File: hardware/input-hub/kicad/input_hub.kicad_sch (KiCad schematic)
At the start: 29 parts, among them J1 ACJMIH, J12 PJ-307, J13 PJ-307, J2 ACJMIH, J5 54602-908LF, J6 BM04B-SRSS-TB_LF__SN_, J7 Conn_01x04, J8 Conn_01x02, J9 XIAO_BAT_SOLDER_ACCESS, P1 B2B-PH-SM4-TB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

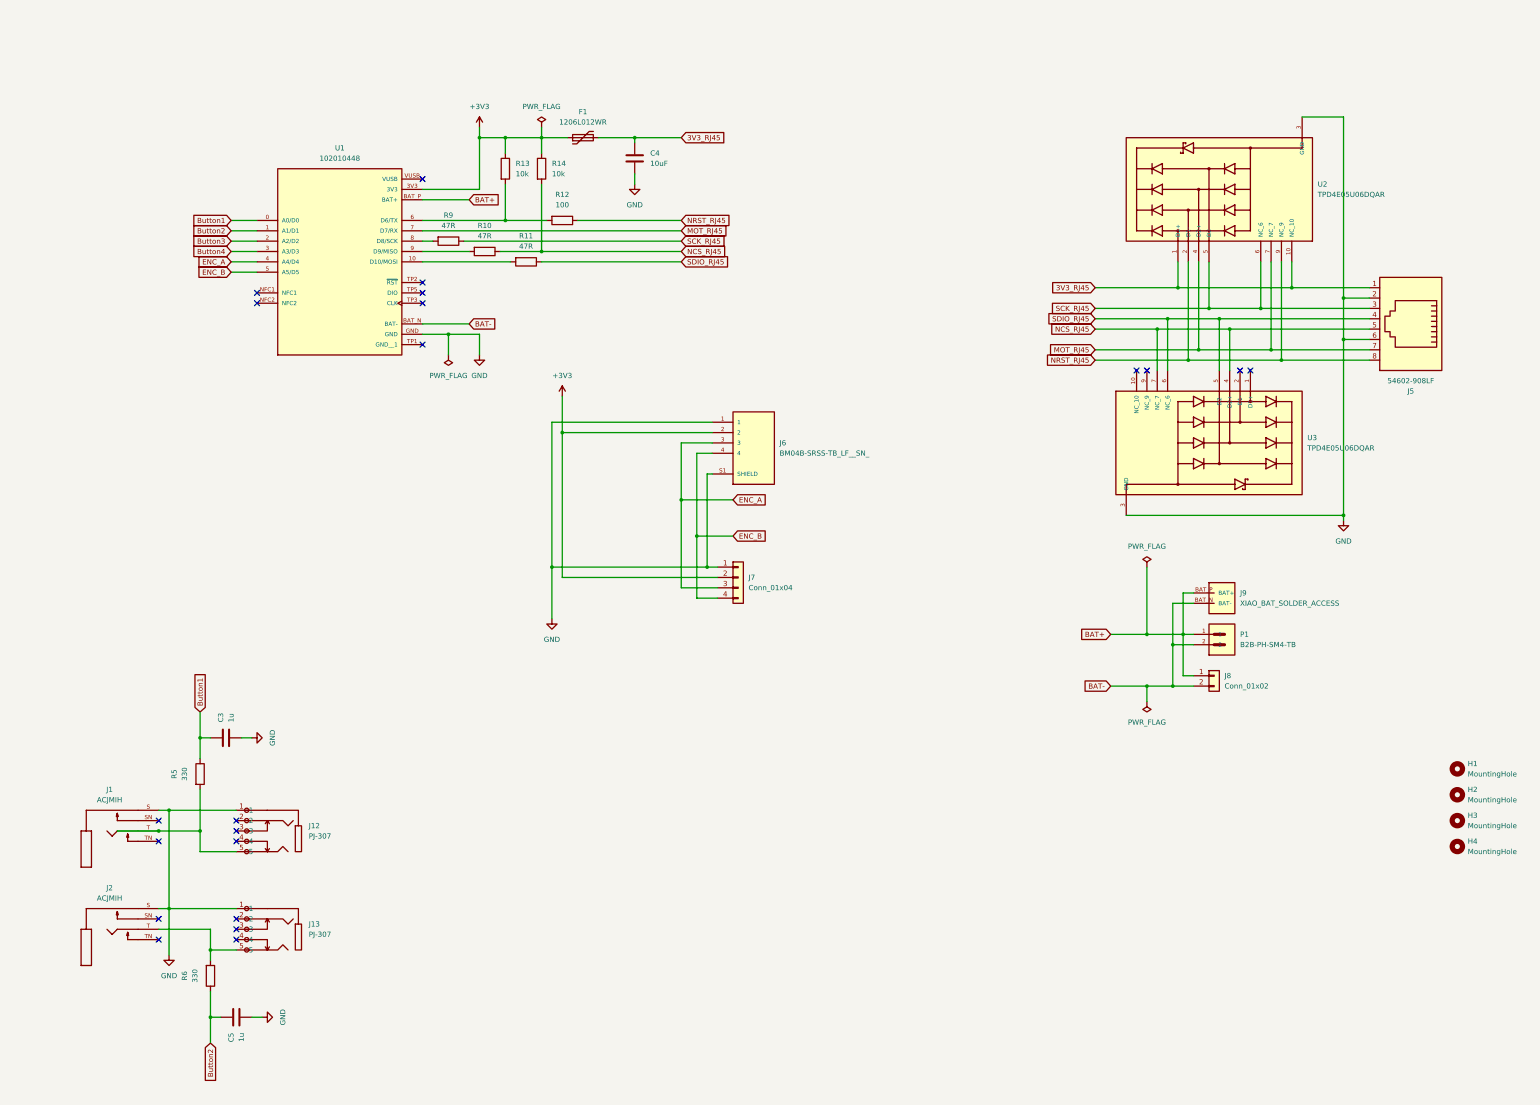
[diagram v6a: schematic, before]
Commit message: feat: prep input hub for JLC assembly
- Add JLC-oriented board constraints, DRC exclusions, revised vias, and production metadata.
  - Add input hub 3D model links, silkscreen logos, PJ-307 footprint updates, and vertical battery
  JST metadata.
  - Route/document PMW3610 reset and MOTION pull-up support with firmware retry configuration.
  - Clean up remaining EC11 encoder library artifacts and stale encoder nets.
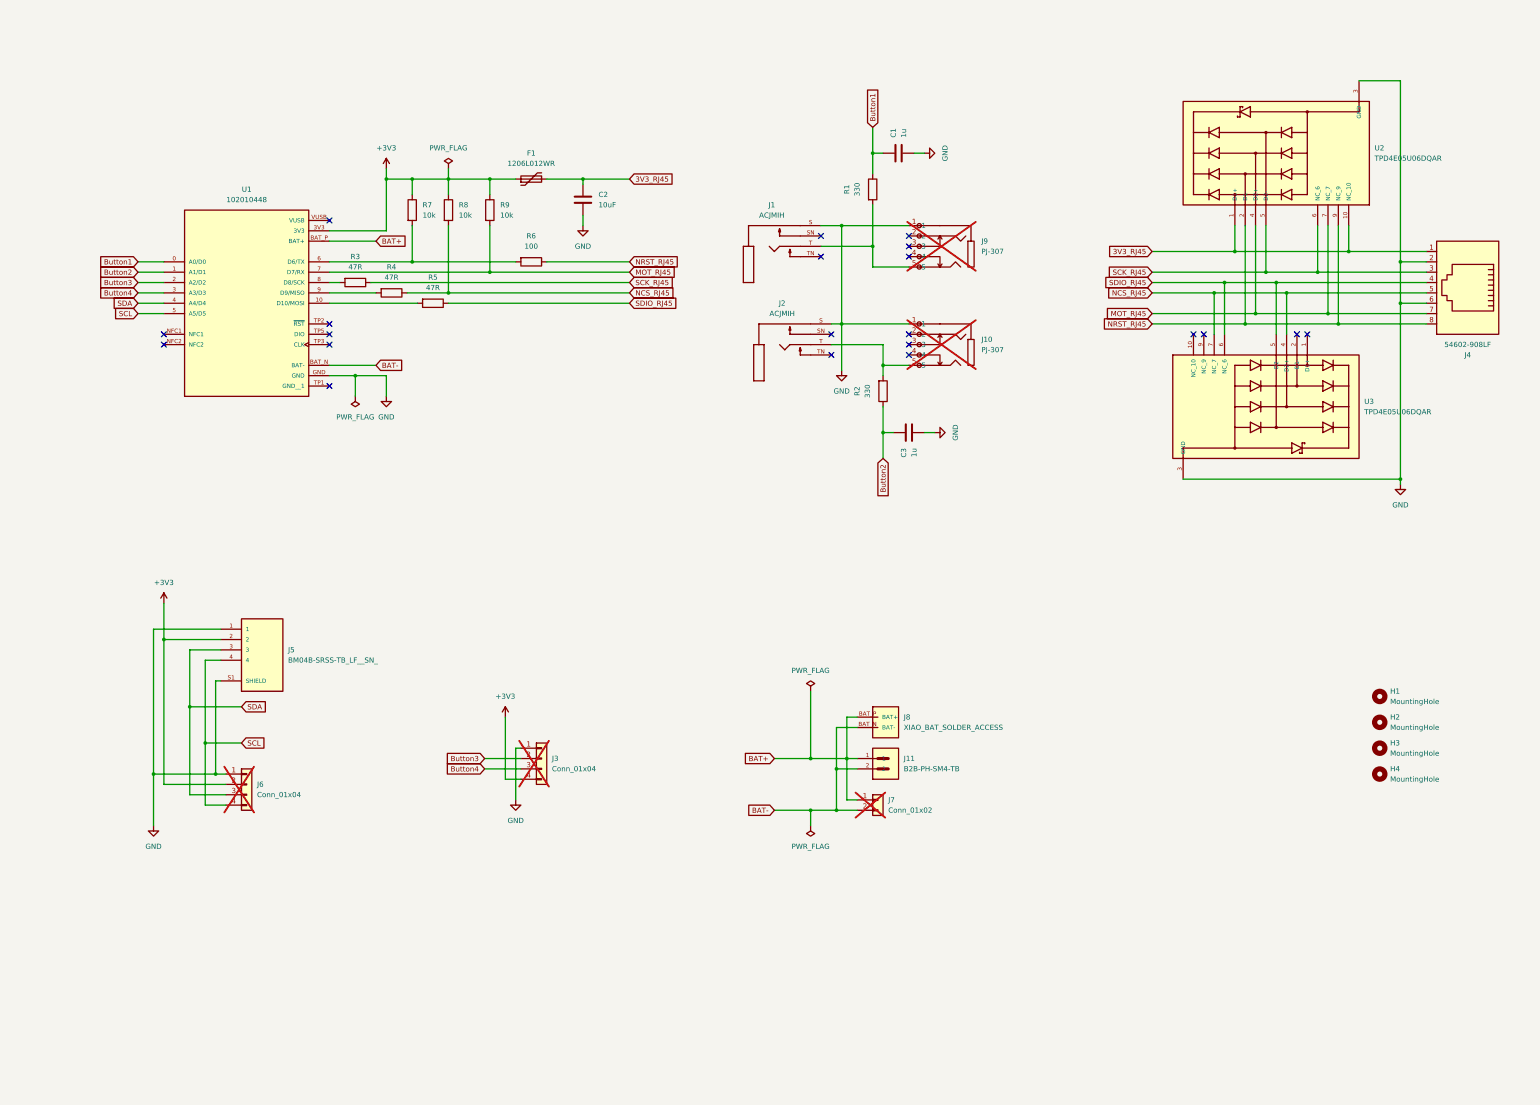
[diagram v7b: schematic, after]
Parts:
- added J3: Conn_01x04, Connector_PinHeader_2.54mm:PinHeader_1x04_P2.54mm_Vertical, symbol Connector_Generic:Conn_01x04
- added R9: 10k, Resistor_SMD:R_0603_1608Metric, symbol Device:R
- C1: renamed from C3; Digi-Key MFR. Part # (none) -> CL10A105KB8NNNC; Digi-Key Part # (none) -> 1276-1860-1-ND; JLCPCB Part # (none) -> C15849; Manufacturer (none) -> Samsung Electro-Mechanics
- C2: renamed from C4; Digi-Key MFR. Part # (none) -> CL21A106KAFN3NE; Digi-Key Part # (none) -> 1276-2890-1-ND; JLCPCB Part # (none) -> C15850; Manufacturer (none) -> Samsung Electro-Mechanics
- C3: renamed from C5; Digi-Key MFR. Part # (none) -> CL10A105KB8NNNC; Digi-Key Part # (none) -> 1276-1860-1-ND; JLCPCB Part # (none) -> C15849; Manufacturer (none) -> Samsung Electro-Mechanics
- F1: Digi-Key MFR. Part # (none) -> 1206L012WR; Digi-Key Part # (none) -> F2864CT-ND; JLCPCB Part # (none) -> C151160; Manufacturer (none) -> Littelfuse
- J1, J2: Digi-Key MFR. Part # (none) -> ACJM-IH; Digi-Key Part # (none) -> 889-ACJM-IH-ND; MFR. Part # (none) -> ACJM-IH; Manufacturer (none) -> Amphenol Audio; now left out of the parts list
- J10: renamed from J13; now not fitted; now left out of the parts list
- J4: renamed from J5; now left out of the parts list
- J5: renamed from J6; Digi-Key MFR. Part # (none) -> BM04B-SRSS-TB(LF)(SN); Digi-Key Part # (none) -> 455-BM04B-SRSS-TBCT-ND; JLCPCB Part # (none) -> C160390; MFR. Part # (none) -> BM04B-SRSS-TB(LF)(SN); Manufacturer (none) -> JST
- J6: renamed from J7; now not fitted; now left out of the parts list
- J7: renamed from J8; now not fitted; now left out of the parts list
- J9: renamed from J12; now not fitted; now left out of the parts list
- R1: renamed from R5; Digi-Key MFR. Part # (none) -> RC0603FR-07330RL; Digi-Key Part # (none) -> 311-330HRCT-ND; JLCPCB Part # (none) -> C23138; Manufacturer (none) -> UNI-ROYAL / DigiKey alt YAGEO
- R2: renamed from R6; Digi-Key MFR. Part # (none) -> RC0603FR-07330RL; Digi-Key Part # (none) -> 311-330HRCT-ND; JLCPCB Part # (none) -> C23138; Manufacturer (none) -> UNI-ROYAL / DigiKey alt YAGEO
- R3: renamed from R9; Digi-Key MFR. Part # (none) -> RC0603FR-0747RL; Digi-Key Part # (none) -> 311-47.0HRCT-ND; JLCPCB Part # (none) -> C23182; Manufacturer (none) -> UNI-ROYAL / DigiKey alt YAGEO
- R4: renamed from R10; Digi-Key MFR. Part # (none) -> RC0603FR-0747RL; Digi-Key Part # (none) -> 311-47.0HRCT-ND; JLCPCB Part # (none) -> C23182; Manufacturer (none) -> UNI-ROYAL / DigiKey alt YAGEO
- R5: renamed from R11; Digi-Key MFR. Part # (none) -> RC0603FR-0747RL; Digi-Key Part # (none) -> 311-47.0HRCT-ND; JLCPCB Part # (none) -> C23182; Manufacturer (none) -> UNI-ROYAL / DigiKey alt YAGEO
- R6: renamed from R12; Digi-Key MFR. Part # (none) -> RC0603FR-07100RL; Digi-Key Part # (none) -> 311-100HRCT-ND; JLCPCB Part # (none) -> C22775; Manufacturer (none) -> UNI-ROYAL / DigiKey alt YAGEO
- R7: renamed from R13; Digi-Key MFR. Part # (none) -> RC0603FR-0710KL; Digi-Key Part # (none) -> 311-10.0KHRCT-ND; JLCPCB Part # (none) -> C25804; Manufacturer (none) -> UNI-ROYAL / DigiKey alt YAGEO
- R8: renamed from R14; Digi-Key MFR. Part # (none) -> RC0603FR-0710KL; Digi-Key Part # (none) -> 311-10.0KHRCT-ND; JLCPCB Part # (none) -> C25804; Manufacturer (none) -> UNI-ROYAL / DigiKey alt YAGEO
- U1: Digi-Key MFR. Part # (none) -> 102010448; Digi-Key Part # (none) -> 1597-102010448-ND; MFR. Part # (none) -> 102010448; Manufacturer (none) -> Seeed Studio; now left out of the parts list
- U2, U3: Digi-Key MFR. Part # (none) -> TPD4E05U06DQAR; Digi-Key Part # (none) -> 296-35765-1-ND; JLCPCB Part # (none) -> C138714; MFR. Part # (none) -> TPD4E05U06DQAR; Manufacturer (none) -> Texas Instruments
- renumbered P1 to J11, J9 to J8
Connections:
- net +3V3: now also J3.4 (Pin_4), R9.1
- net Button3: now also J3.2 (Pin_2)
- net Button4: now also J3.3 (Pin_3)
- net GND: now also J3.1 (Pin_1)
- net MOT_RJ45: now also R9.2
- net ENC_A renamed SDA
- net ENC_B renamed SCL
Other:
- moved on the sheet: C1, C2, C3, F1, H1, H2, H3, H4, J1, J11, J2, J4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

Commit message: fix: add input hub pedal normal jumpers
- Route pedal jack normal contacts
  through optional 0R jumpers to ground.
  - Use existing 0603 0R jumper sourcing for the new input hub build options.
  - Track release-ready input hub fabrication outputs for ordering.
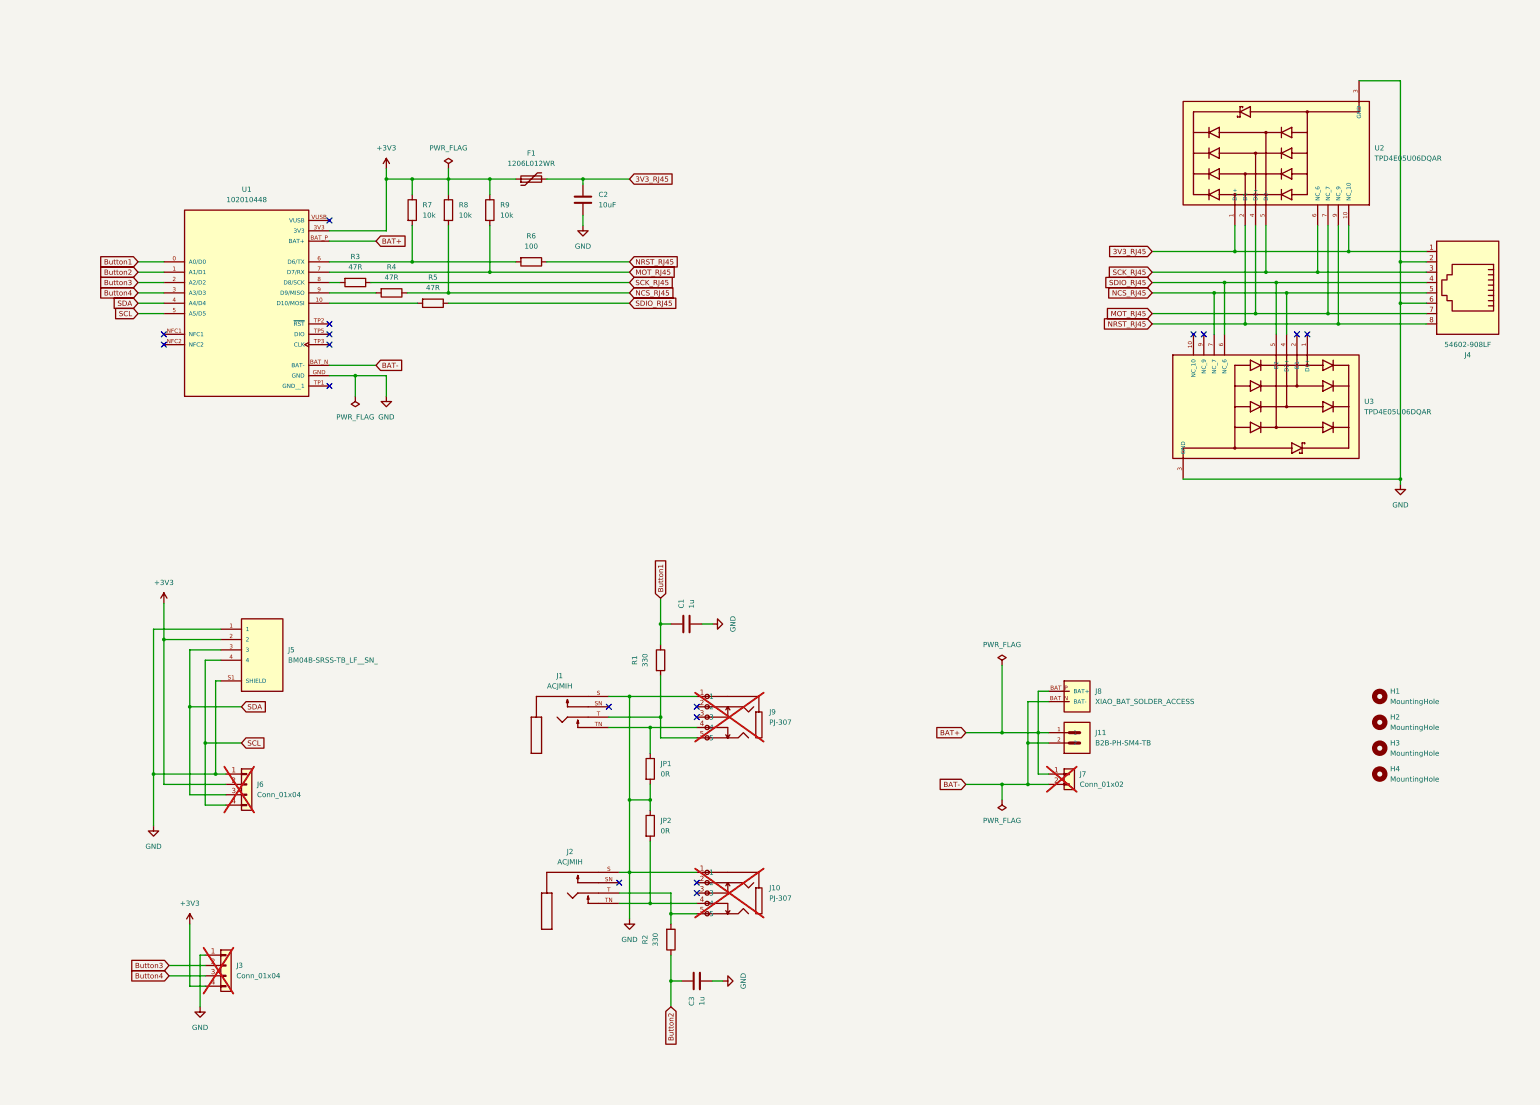
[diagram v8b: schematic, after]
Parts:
- added JP1, JP2: 0R, Resistor_SMD:R_0603_1608Metric, symbol Device:R
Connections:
- net GND: now also JP1.2, JP2.1
- net at J9.4: now also J1.TN, JP1.1
- net at J10.4: now also J2.TN, JP2.2
- no-connect marks 21 -> 17
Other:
- moved on the sheet: C1, C3, J1, J10, J11, J2, J3, J7, J8, J9, R1, R2
